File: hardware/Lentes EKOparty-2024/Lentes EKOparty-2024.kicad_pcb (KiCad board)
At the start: 2 copper layers, 43.8 x 8.6 mm, 2 parts

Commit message: feat(Hw):Added_Shitty_Add-on
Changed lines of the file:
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@@
 			)
 			(fill solid)
-			(layer "F.SilkS")
+			(layer "B.Paste")
+		)
+		(fp_poly
+			(pts
+				(xy 14.8145 -0.029452) (xy 16.253834 -0.029452) (xy 16.253834 -1.426452) (xy 16.996931 -1.426452)
+				(xy 17.19752 -1.426226) (xy 17.359503 -1.425449) (xy 17.486604 -1.423973) (xy 17.582548 -1.421651)
+				(xy 17.65106 -1.418334) (xy 17.695866 -1.413875) (xy 17.72069 -1.408126) (xy 17.729256 -1.40094)
+				(xy 17.728884 -1.397408) (xy 17.710673 -1.328809) (xy 17.702797 -1.240905) (xy 17.705327 -1.127957)
+				(xy 17.718333 -0.984225) (xy 17.735721 -0.847603) (xy 17.761287 -0.631195) (xy 17.77423 -0.443935)
+				(xy 17.774591 -0.288381) (xy 17.762409 -0.167094) (xy 17.737723 -0.082633) (xy 17.723609 -0.05872)
+				(xy 17.673195 -0.002239) (xy 17.621531 0.043323) (xy 17.550903 0.074599) (xy 17.441481 0.091774)
+				(xy 17.292992 0.09485) (xy 17.105162 0.083833) (xy 16.877719 0.058726) (xy 16.846729 0.05463) (xy 16.694412 0.035445)
+				(xy 16.577094 0.02384) (xy 16.488199 0.019404) (xy 16.421155 0.021725) (xy 16.389358 0.026067) (xy 16.285584 0.045014)
+				(xy 16.275 0.710915) (xy 16.264417 1.376817) (xy 16.170174 1.395442) (xy 16.089615 1.40254) (xy 15.974951 1.399759)
+				(xy 15.842091 1.388248) (xy 15.671976 1.369786) (xy 15.537605 1.35614) (xy 15.432702 1.346962) (xy 15.350994 1.341904)
+				(xy 15.286207 1.340618) (xy 15.232066 1.342757) (xy 15.182299 1.34797) (xy 15.16375 1.350607) (xy 15.030779 1.384367)
+				(xy 14.928899 1.442615) (xy 14.856197 1.527917) (xy 14.810763 1.642842) (xy 14.790686 1.789955)
+				(xy 14.789302 1.853478) (xy 14.792886 1.966571) (xy 14.801776 2.089601) (xy 14.814131 2.197738)
+				(xy 14.815543 2.207143) (xy 14.827758 2.305545) (xy 14.836721 2.416168) (xy 14.842162 2.528898)
+				(xy 14.843812 2.633623) (xy 14.841405 2.720232) (xy 14.834671 2.778612) (xy 14.831039 2.791006)
+				(xy 14.824275 2.801132) (xy 14.810319 2.809234) (xy 14.784863 2.815535) (xy 14.743599 2.82026) (xy 14.682219 2.823631)
+				(xy 14.596414 2.825871) (xy 14.481878 2.827205) (xy 14.3343 2.827855) (xy 14.149375 2.828045) (xy 14.116664 2.828048)
+				(xy 13.4175 2.828048) (xy 13.4175 1.395072) (xy 13.264042 1.404775) (xy 13.139042 1.404409) (xy 12.97857 1.39018)
+				(xy 12.818381 1.367591) (xy 12.625282 1.340322) (xy 12.467697 1.327204) (xy 12.340971 1.329021)
+				(xy 12.240452 1.346559) (xy 12.161484 1.3806) (xy 12.099413 1.431932) (xy 12.05225 1.49676) (xy 12.027015 1.566235)
+				(xy 12.012951 1.670867) (xy 12.010052 1.811957) (xy 12.018309 1.990807) (xy 12.037715 2.208719)
+				(xy 12.047648 2.298881) (xy 12.064492 2.465884) (xy 12.072613 2.597238) (xy 12.071901 2.690652)
+				(xy 12.068234 2.722215) (xy 12.051089 2.817465) (xy 11.305545 2.823027) (xy 10.56 2.828589) (xy 10.56 1.43)
+				(xy 10.614295 1.409357) (xy 10.693341 1.393367) (xy 10.811948 1.390253) (xy 10.969355 1.399984)
+				(xy 11.164805 1.422532) (xy 11.240929 1.43328) (xy 11.447933 1.458652) (xy 11.618785 1.467577) (xy 11.756781 1.458969)
+				(xy 11.865217 1.43174) (xy 11.947391 1.384801) (xy 12.0066 1.317066) (xy 12.046139 1.227447) (xy 12.061848 1.162421)
+				(xy 12.068351 1.122069) (xy 12.072057 1.080083) (xy 12.072547 1.030782) (xy 12.0694 0.968487) (xy 12.062194 0.887518)
+				(xy 12.05051 0.782193) (xy 12.033927 0.646833) (xy 12.012024 0.475758) (xy 12.009643 0.457381) (xy 11.992275 0.296695)
+				(xy 11.986884 0.173729) (xy 11.993115 0.086965) (xy 12.010886 -0.018869) (xy 13.4175 -0.030023)
+				(xy 13.4175 -1.426452) (xy 14.8145 -1.426452) (xy 14.8145 -0.029452)
+			)
+			(stroke
+				(width 0.01)
+				(type solid)
+			)
+			(fill solid)
+			(layer "B.Paste")
+		)
+		(fp_poly
+			(pts
+				(xy -7.750845 -0.026501) (xy -6.311512 -0.026501) (xy -6.311512 -1.423501) (xy -5.568414 -1.423501)
+				(xy -5.367825 -1.423275) (xy -5.205843 -1.422498) (xy -5.078742 -1.421022) (xy -4.982798 -1.4187)
+				(xy -4.914285 -1.415383) (xy -4.86948 -1.410924) (xy -4.844656 -1.405175) (xy -4.836089 -1.397989)
+				(xy -4.836461 -1.394457) (xy -4.854672 -1.325858) (xy -4.862549 -1.237954) (xy -4.860019 -1.125006)
+				(xy -4.847012 -0.981274) (xy -4.829624 -0.844652) (xy -4.804059 -0.628244) (xy -4.791115 -0.440984)
+				(xy -4.790754 -0.28543) (xy -4.802936 -0.164143) (xy -4.827622 -0.079682) (xy -4.841737 -0.055769)
+				(xy -4.892151 0.000712) (xy -4.943815 0.046274) (xy -5.014443 0.07755) (xy -5.123865 0.094725) (xy -5.272354 0.097801)
+				(xy -5.460183 0.086784) (xy -5.687627 0.061677) (xy -5.718617 0.057581) (xy -5.870934 0.038396)
+				(xy -5.988252 0.026791) (xy -6.077146 0.022355) (xy -6.144191 0.024676) (xy -6.175988 0.029018)
+				(xy -6.279762 0.047965) (xy -6.290345 0.714523) (xy -6.300929 1.381082) (xy -6.402951 1.400781)
+				(xy -6.454688 1.406821) (xy -6.524367 1.40746) (xy -6.617751 1.402367) (xy -6.740604 1.391208) (xy -6.89869 1.373651)
+				(xy -6.923454 1.370724) (xy -7.074688 1.353311) (xy -7.191211 1.341506) (xy -7.280229 1.33497) (xy -7.348946 1.333365)
+				(xy -7.404564 1.33635) (xy -7.454288 1.343586) (xy -7.463156 1.345312) (xy -7.592075 1.385684) (xy -7.687175 1.449056)
+				(xy -7.745321 1.525626) (xy -7.768343 1.598825) (xy -7.78 1.71) (xy -7.780301 1.856354) (xy -7.769261 2.035088)
+				(xy -7.746891 2.243402) (xy -7.74208 2.280666) (xy -7.721855 2.457619) (xy -7.713116 2.595764) (xy -7.715753 2.697003)
+				(xy -7.717145 2.709291) (xy -7.732725 2.830999) (xy -9.145252 2.830999) (xy -9.158411 2.741041)
+				(xy -9.161717 2.689163) (xy -9.162264 2.604602) (xy -9.160195 2.496909) (xy -9.155652 2.375633)
+				(xy -9.151882 2.301832) (xy -9.143636 2.110076) (xy -9.143135 1.954642) (xy -9.15093 1.830135) (xy -9.16757 1.731159)
+				(xy -9.193607 1.652319) (xy -9.223832 1.596659) (xy -9.299037 1.518871) (xy -9.405599 1.457847)
+				(xy -9.535983 1.413636) (xy -9.682653 1.386288) (xy -9.838072 1.375852) (xy -9.994704 1.382378)
+				(xy -10.145014 1.405915) (xy -10.281464 1.446512) (xy -10.396519 1.50422) (xy -10.482642 1.579088)
+				(xy -10.490005 1.588345) (xy -10.529623 1.648805) (xy -10.559951 1.717217) (xy -10.581774 1.799254)
+				(xy -10.595875 1.900583) (xy -10.603036 2.026878) (xy -10.604043 2.183806) (xy -10.599677 2.377039)
+				(xy -10.599543 2.381207) (xy -10.585089 2.830999) (xy -12.005345 2.830999) (xy -12.005345 1.432951)
+				(xy -11.951051 1.412308) (xy -11.872004 1.396318) (xy -11.753398 1.393204) (xy -11.59599 1.402935)
+				(xy -11.400541 1.425483) (xy -11.324417 1.436231) (xy -11.116167 1.461666) (xy -10.944175 1.470416)
+				(xy -10.80534 1.461392) (xy -10.696563 1.433503) (xy -10.614744 1.385658) (xy -10.556783 1.316766)
+				(xy -10.519581 1.225736) (xy -10.504138 1.147578) (xy -10.498632 1.100276) (xy -10.495812 1.05289)
+				(xy -10.496138 0.9992) (xy -10.500071 0.932986) (xy -10.508073 0.848031) (xy -10.520605 0.738115)
+				(xy -10.538128 0.597019) (xy -10.554324 0.470859) (xy -10.571918 0.310829) (xy -10.578297 0.188112)
+				(xy -10.573622 0.099244) (xy -10.572187 0.089859) (xy -10.55446 -0.015918) (xy -9.851153 -0.021495)
+				(xy -9.147845 -0.027072) (xy -9.147845 -1.423501) (xy -7.750845 -1.423501) (xy -7.750845 -0.026501)
+			)
+			(stroke
+				(width 0.01)
+				(type solid)
+			)
+			(fill solid)
+			(layer "F.Paste")
 		)
 		(fp_poly
@@
 			)
 			(fill solid)
-			(layer "F.SilkS")
+			(layer "F.Paste")
 		)
 		(fp_poly

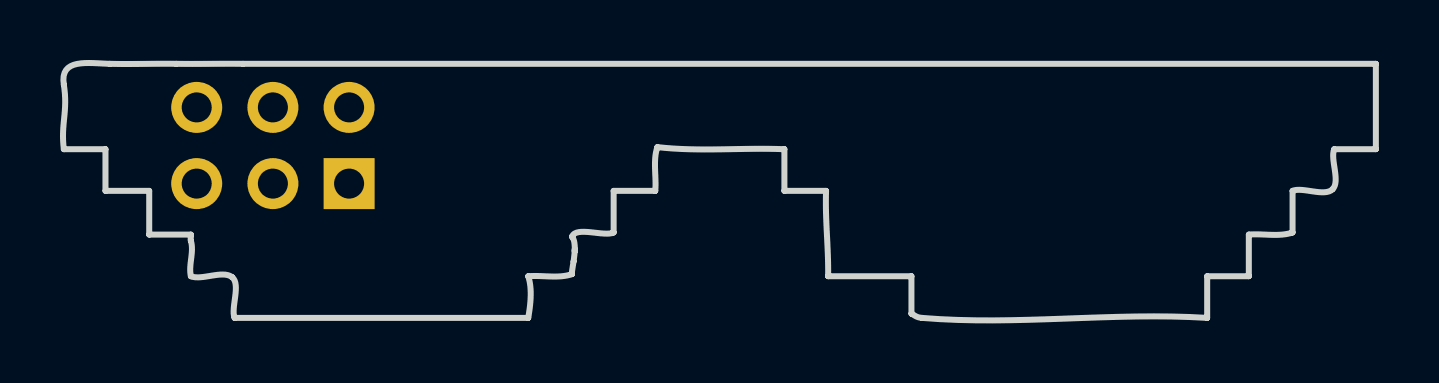
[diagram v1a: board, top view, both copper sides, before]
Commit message: feat(Hw):Update_Lentes
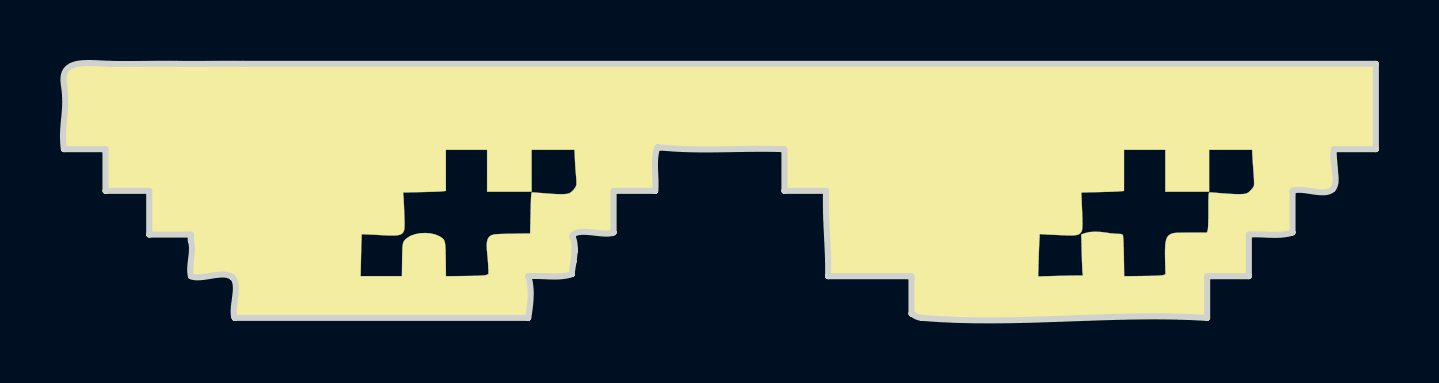
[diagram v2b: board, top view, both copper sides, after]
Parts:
- added Ref**: Val**, Eko2024:llama-2-flaca, F.Cu at (129.0, 65.0)

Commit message: feat(Hw): Update lentes
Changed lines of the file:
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@@
 	(footprint "Eko2024:llama-2-flaca"
 		(layer "F.Cu")
-		(at 129.02 64.96)
+		(at 128.99 64.93)
 		(property "Reference" "Ref**"
 			(at 0 0 0)
@@
 	(footprint "Eko2024:llama intermedia_Contorno"
 		(layer "F.Cu")
-		(at 129.01 64.95)
+		(at 129 64.93)
 		(property "Reference" "Ref**"
 			(at 0 0 0)
@@
 		(net 0)
 		(net_name "")
-		(layer "Edge.Cuts")
+		(layers "F&B.Cu")
 		(hatch edge 0.5)
 		(connect_pads
@@
 		(filled_areas_thickness no)
 		(keepout
-			(tracks not_allowed)
-			(vias not_allowed)
-			(pads not_allowed)
+			(tracks allowed)
+			(vias allowed)
+			(pads allowed)
 			(copperpour not_allowed)
 			(footprints allowed)
@@
 		(polygon
 			(pts
-				(xy 107.13 60.71) (xy 150.855558 60.697123) (xy 150.88 69.38) (xy 107.12 69.38) (xy 107.1 60.7)
-			)
-		)
+				(xy 146.96 63.3) (xy 142.16 63.29) (xy 142.16 64.76) (xy 140.87 64.76) (xy 140.86 66.15) (xy 139.28 66.2)
+				(xy 139.29 67.9) (xy 144.15 67.94) (xy 144.16 66.53) (xy 145.39 66.52) (xy 145.41 65.23) (xy 146.96 65.24)
+			)
+		)
+	)
+	(zone
+		(net 0)
+		(net_name "")
+		(layers "F&B.Cu")
+		(hatch edge 0.5)
+		(connect_pads
+			(clearance 0)
+		)
+		(min_thickness 0.25)
+		(filled_areas_thickness no)
+		(keepout
+			(tracks allowed)
+			(vias allowed)
+			(pads allowed)
+			(copperpour not_allowed)
+			(footprints allowed)
+		)
+		(fill
+			(thermal_gap 0.5)
+			(thermal_bridge_width 0.5)
+		)
+		(polygon
+			(pts
+				(xy 124.33 63.35) (xy 119.37 63.33) (xy 119.32 64.67) (xy 118.1 64.7) (xy 118 66.15) (xy 116.25 66.1)
+				(xy 116.26 68.05) (xy 121.78 68.03) (xy 121.78 66.58) (xy 123.01 66.58) (xy 123.06 65.29) (xy 124.33 65.24)
+			)
+		)

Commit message: feat(Hw):Update_BoM
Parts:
- removed REF**: PinHeader_2x03_P2.54mm_Vertical, Connector_PinHeader_2.54mm:PinHeader_2x03_P2.54mm_Vertical
- added J2: Conn_02x03_Odd_Even, Connector_PinHeader_2.54mm:PinHeader_2x03_P2.54mm_Vertical, B.Cu at (116.6, 64.7)
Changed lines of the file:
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@@
 	)
 	(net 0 "")
+	(net 1 "unconnected-(J2-Pin_2-Pad2)")
+	(net 2 "unconnected-(J2-Pin_4-Pad4)")
+	(net 3 "unconnected-(J2-Pin_5-Pad5)")
+	(net 4 "unconnected-(J2-Pin_3-Pad3)")
+	(net 5 "unconnected-(J2-Pin_1-Pad1)")
+	(net 6 "unconnected-(J2-Pin_6-Pad6)")
 	(footprint "Eko2024:llama-2-flaca"
 		(layer "F.Cu")
@@
 		(descr "Through hole straight pin header, 2x03, 2.54mm pitch, double rows")
 		(tags "Through hole pin header THT 2x03 2.54mm double row")
-		(property "Reference" "REF**"
+		(property "Reference" "J2"
 			(at 1.27 2.33 90)
 			(layer "B.SilkS")
@@
 			)
 		)
-		(property "Value" "PinHeader_2x03_P2.54mm_Vertical"
+		(property "Value" "Conn_02x03_Odd_Even"
 			(at 1.27 -7.41 90)
 			(layer "B.Fab")
@@
 			)
 		)
-		(property "Description" ""
+		(property "Description" "Generic connector, double row, 02x03, odd/even pin numbering scheme (row 1 odd numbers, row 2 even numbers), script generated (kicad-library-utils/schlib/autogen/connector/)"
 			(at 0 0 -90)
 			(unlocked yes)
@@
 			)
 		)
+		(property ki_fp_filters "Connector*:*_2x??_*")
+		(sheetname "Raíz")
+		(sheetfile "Lentes EKOparty-2024.kicad_sch")
 		(attr through_hole)
 		(fp_line
@@
 		)
 		(fp_text user "${REFERENCE}"
-			(at 1.27 -2.54 0)
+			(at 1.27 -2.54 360)
 			(layer "B.Fab")
 			(effects
@@
 			(layers "*.Cu" "*.Mask")
 			(remove_unused_layers no)
+			(net 5 "unconnected-(J2-Pin_1-Pad1)")
+			(pinfunction "Pin_1")
+			(pintype "passive+no_connect")
 		)
 		(pad "2" thru_hole oval
@@
 			(layers "*.Cu" "*.Mask")
 			(remove_unused_layers no)
+			(net 1 "unconnected-(J2-Pin_2-Pad2)")
+			(pinfunction "Pin_2")
+			(pintype "passive+no_connect")
 		)
 		(pad "3" thru_hole oval
@@
 			(layers "*.Cu" "*.Mask")
 			(remove_unused_layers no)
+			(net 4 "unconnected-(J2-Pin_3-Pad3)")
+			(pinfunction "Pin_3")
+			(pintype "passive+no_connect")
 		)
 		(pad "4" thru_hole oval
@@
 			(layers "*.Cu" "*.Mask")
 			(remove_unused_layers no)
+			(net 2 "unconnected-(J2-Pin_4-Pad4)")
+			(pinfunction "Pin_4")
+			(pintype "passive+no_connect")
 		)
 		(pad "5" thru_hole oval
@@
 			(layers "*.Cu" "*.Mask")
 			(remove_unused_layers no)
+			(net 3 "unconnected-(J2-Pin_5-Pad5)")
+			(pinfunction "Pin_5")
+			(pintype "passive+no_connect")
 		)
 		(pad "6" thru_hole oval
@@
 			(layers "*.Cu" "*.Mask")
 			(remove_unused_layers no)
+			(net 6 "unconnected-(J2-Pin_6-Pad6)")
+			(pinfunction "Pin_6")
+			(pintype "passive+no_connect")
 		)
 		(model "${KICAD8_3DMODEL_DIR}/Connector_PinHeader_2.54mm.3dshapes/PinHeader_2x03_P2.54mm_Vertical.wrl"

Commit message: feat: add logo pcbway
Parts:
- added G***: LOGO, LOGO, B.Cu at (136.8, 63.7)
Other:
- board text added: "Sponsored by"
